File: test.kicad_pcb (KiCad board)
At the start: 4 copper layers, 100 x 50 mm, 110 parts, among them IC1 USBLC6-2SC6, IC2 AD9288BSTZ-40, IC3 MAX17048G+T10, IC4 BQ24074RGTR, IC5 TCA9534APWR, IC6 MCP6S91-E_MS, IC7 MCP6S91-E_MS, IC8 MCP4726A0T-E_CH, J1 PWM, K1 AQY210EHAX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

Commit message: routing
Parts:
- moved SW3 118.0 mm to (114.5, 94.7), turned to 90 degrees
- moved Q1 21.6 mm to (119.0, 85.4)
- moved R15 21.6 mm to (115.5, 86.4)
- moved Q2 21.6 mm to (119.0, 81.8)
- moved R8 21.6 mm to (115.5, 82.8)
- moved R11 20.1 mm to (131.8, 69.6), turned to -90 degrees
- moved IC1 18.4 mm to (113.5, 74.2), turned to 180 degrees
- moved R9 16.5 mm to (134.9, 61.5)
- moved JP1 15.7 mm to (106.9, 66.8), turned to 90 degrees
- moved C15 14.6 mm to (133.2, 61.5)
- moved IC4 12.8 mm to (128.4, 62.6)
- moved C14 12.8 mm to (128.3, 65.6)
- moved C17 12.8 mm to (125.4, 63.1)
- moved R6 11.9 mm to (114.8, 59.3), turned to 90 degrees
- moved R10 11.7 mm to (125.4, 66.5), turned to -90 degrees
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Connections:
- C10 pad 2: GNDA -> GND
- C20 pad 2: GNDA -> GND
- C22 pad 2: GNDA -> GND
- C3 pad 2: GNDA -> GND
- C30 pad 2: GNDA -> GND
- C31 pad 2: GNDA -> GND
- C32 pad 2: GNDA -> GND
- C9 pad 2: GNDA -> GND
- D10 pad 2: GNDA -> GND
- D6 pad 1: GNDA -> GND
- D8 pad 2: GNDA -> GND
- IC2 pad 1: GNDA -> GND
- IC2 pad 10: GNDA -> GNDREF
- IC2 pad 29: GNDA -> GND
- IC2 pad 3: GNDA -> GNDREF
- IC2 pad 32: GNDA -> GND
- IC6 pad 4: GNDA -> GND
- IC7 pad 4: GNDA -> GND
- IC8 pad 2: GNDA -> GND
- R20 pad 1: GNDA -> GND
- R21 pad 1: GNDA -> GND
- U10 pad 4: GNDA -> GND
- U3 pad 13: /CH1_D6 -> /CH2_D6
- U3 pad 14: /CH1_D7 -> /CH2_D7
- U3 pad 24: /CH2_D0 -> /CH1_D7
- U3 pad 26: /CH2_D1 -> /CH1_D6
- U3 pad 27: /CH2_D3 -> /CH1_D5
- U3 pad 28: /CH2_D4 -> /CH1_D4
- U3 pad 29: /CH2_D2 -> /CH1_D3
- U3 pad 30: /CH2_D5 -> /CH1_D2
- U3 pad 31: /CH2_D6 -> /CH1_D1
- U3 pad 37: /CH2_D7 -> /CH1_D0
- U3 pad 4: /CH1_D0 -> /CH2_D0
- U3 pad 5: /CH1_D1 -> /CH2_D1
- U3 pad 6: /CH1_D2 -> /CH2_D2
- U3 pad 7: /CH1_D3 -> /CH2_D3
- U3 pad 8: /CH1_D4 -> /CH2_D4
- U3 pad 9: /CH1_D5 -> /CH2_D5
- U7 pad 1: GNDA -> GND
- U8 pad 4: GNDA -> GND
- U9 pad 4: GNDA -> GND
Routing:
- net GND: track 114.2 -> 320.4 mm, vias 0 -> 28
- net GNDREF: track 69.6 -> 137.4 mm, vias 0 -> 1
- net Net-(C19-Pad1): track 5.91 -> 68.1 mm, vias 0 -> 3
- net Net-(C15-Pad1): track 4.26 -> 64.2 mm, vias 0 -> 1
- net +5V: track 16.2 -> 71.5 mm
- net Offset_CH2: track 3.21 -> 58.3 mm, vias 0 -> 1
- net Offset_CH1: track 3.51 -> 57.5 mm, vias 0 -> 1
- net Trigger_CH1: track 0.00 -> 49.5 mm, vias 0 -> 2
- net Trigger_CH2: track 0.00 -> 48.3 mm, vias 0 -> 2
- net +3V3: track 101.9 -> 148.9 mm, vias 2 -> 9
- net IO0: track 8.03 -> 54.7 mm, vias 0 -> 2
- net Net-(C17-Pad1): track 2.50 -> 48.3 mm, vias 0 -> 3
- net GNDA: track 45.7 -> 0.00 mm, vias 10 -> 0
- net SCL_I2C: track 45.6 -> 89.9 mm, vias 0 -> 4
- net /CH1_D0: track 0.00 -> 40.2 mm, vias 0 -> 2
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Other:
- board text added: "JLCJLCJLC"

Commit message: last changes
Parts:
- removed D10, D9: D_Schottky, Diode_SMD:D_0805_2012Metric_Pad1.15x1.40mm_HandSolder
- added C23: 4.7u, Capacitor_SMD:C_0603_1608Metric_Pad1.08x0.95mm_HandSolder, F.Cu at (123.0, 64.3)
- added G***: LOGO, project_library:test, F.Cu at (111.6, 51.7)
- added TP12: SCLK_I2C, TestPoint:TestPoint_Keystone_5000-5004_Miniature, F.Cu at (158.7, 95.2)
- added TP13: SDA, TestPoint:TestPoint_Keystone_5000-5004_Miniature, F.Cu at (155.2, 95.2)
- added TP14: MOSI, TestPoint:TestPoint_Keystone_5000-5004_Miniature, F.Cu at (169.8, 85.7)
- added TP15: SCLK_SPI, TestPoint:TestPoint_Keystone_5000-5004_Miniature, F.Cu at (162.2, 82.4)
- added TP16: TX, TestPoint:TestPoint_Keystone_5000-5004_Miniature, F.Cu at (118.5, 89.5)
- added TP17: RX, TestPoint:TestPoint_Keystone_5000-5004_Miniature, F.Cu at (122.7, 70.5)
- D7, D8: value D_Schottky -> BAT54S; footprint Diode_SMD:D_0805_2012Metric_Pad1.15x1.40mm_HandSolder -> Package_TO_SOT_SMD:SOT-23
- moved D7 4.88 mm to (190.6, 69.4)
- moved D8 4.09 mm to (190.6, 73.5)
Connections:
- D7 pad 1: +3.3VA -> GND
- D7 pad 2: Net-(C26-Pad1) -> +3.3VA
- D8 pad 1: Net-(C26-Pad1) -> GND
- D8 pad 2: GND -> +3.3VA
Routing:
- net +3V3: track 148.9 -> 107.6 mm
- net SDA: track 84.1 -> 96.1 mm
- net RX: track 26.7 -> 34.3 mm
- net SCL_I2C: track 89.9 -> 97.3 mm
- net MOSI: track 32.7 -> 39.3 mm
- net TX: track 27.4 -> 33.7 mm
- net Net-(IC1-Pad6): track 6.36 -> 12.6 mm, vias 0 -> 2
- net Net-(C17-Pad1): track 48.3 -> 52.7 mm
- net GND: track 320.4 -> 324.5 mm, vias 28 -> 29
- net SCLK_SPI: track 29.3 -> 33.4 mm
- net Net-(C27-Pad1): track 36.7 -> 34.4 mm
- net +5V: track 71.5 -> 70.3 mm
- net +3.3VA: track 68.6 -> 69.4 mm
- net Offset_CH2: track 58.3 -> 59.1 mm
- net Net-(C15-Pad1): track 64.2 -> 64.9 mm
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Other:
- outline, holes or cut-outs redrawn
- board text added: "TH/MO"

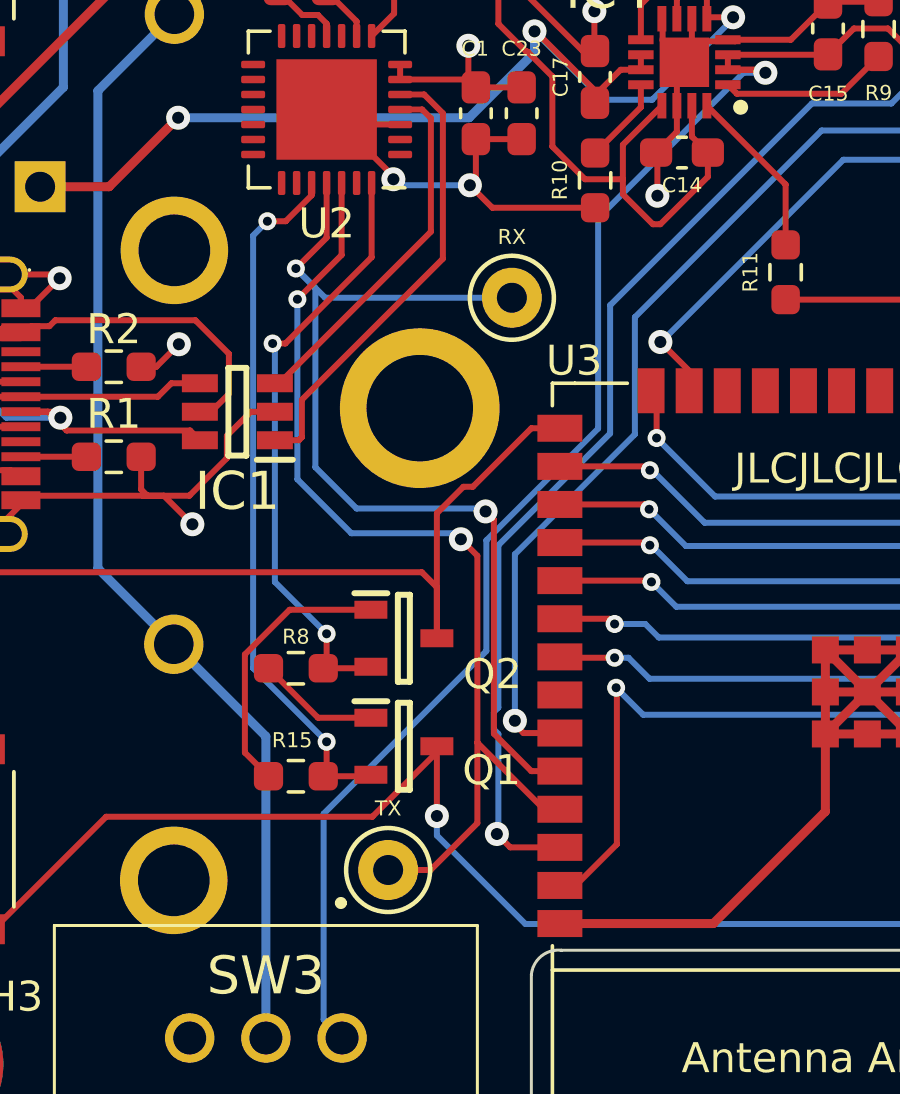
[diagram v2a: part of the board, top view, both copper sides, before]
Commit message: fixed uart connection
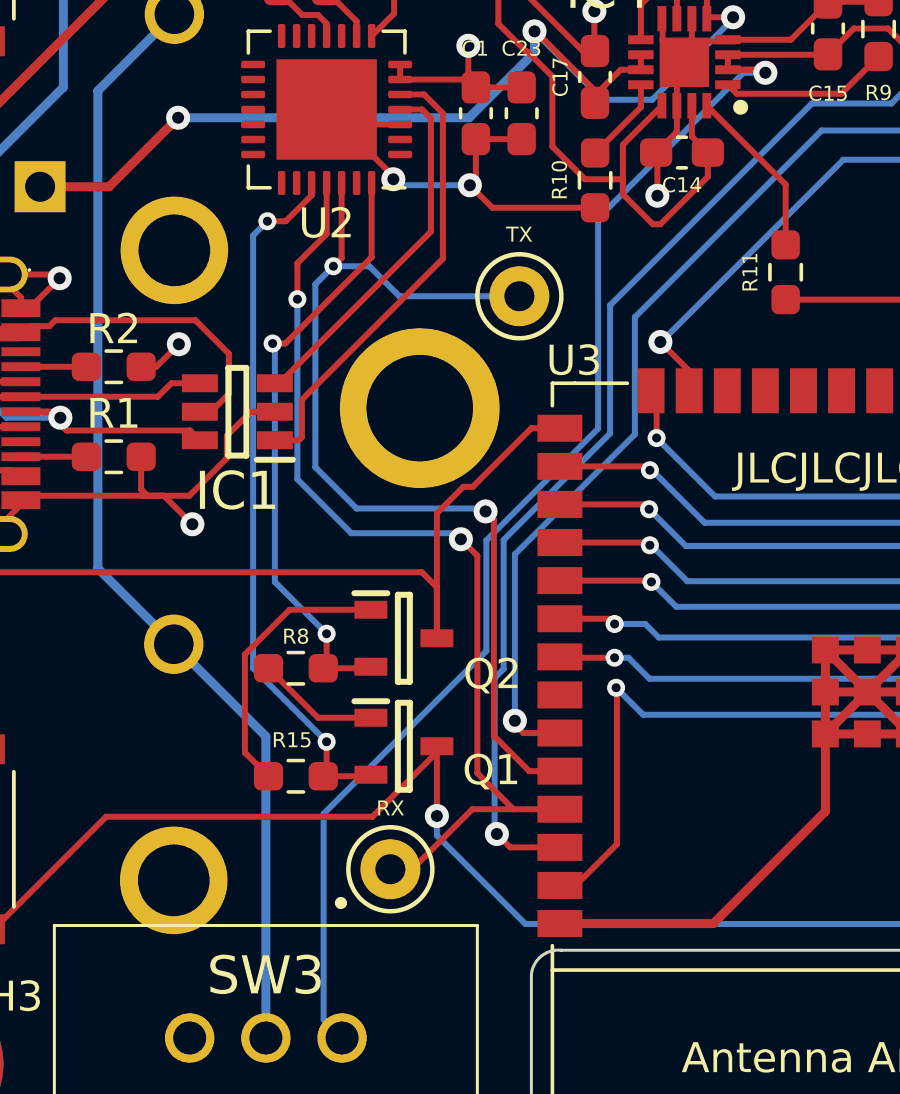
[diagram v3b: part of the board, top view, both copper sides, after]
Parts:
- moved TP16 19.6 mm to (122.9, 70.4)
- moved TP17 19.5 mm to (118.6, 89.5)
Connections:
- U3 pad 34: RX -> TX
- U3 pad 35: TX -> RX
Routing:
- net RX: track 34.3 -> 32.8 mm
- net TX: track 33.7 -> 33.0 mm
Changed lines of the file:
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@@
       (net 46 "SDA") (pinfunction "GPIO21") (pintype "bidirectional"))
     (pad "34" smd rect locked (at 8.75 -1.93) (size 1.5 0.9) (layers "F.Cu" "F.Paste" "F.Mask")
-      (net 5 "RX") (pinfunction "U0RXD/GPIO3") (pintype "bidirectional"))
+      (net 56 "TX") (pinfunction "U0RXD/GPIO3") (pintype "bidirectional"))
     (pad "35" smd rect locked (at 8.75 -3.2) (size 1.5 0.9) (layers "F.Cu" "F.Paste" "F.Mask")
-      (net 56 "TX") (pinfunction "U0TXD/GPIO1") (pintype "bidirectional"))
+      (net 5 "RX") (pinfunction "U0TXD/GPIO1") (pintype "bidirectional"))
     (pad "36" smd rect locked (at 8.75 -4.47) (size 1.5 0.9) (layers "F.Cu" "F.Paste" "F.Mask")
       (net 45 "SCL_I2C") (pinfunction "GPIO22") (pintype "bidirectional"))
@@
   )
   (footprint "TestPoint:TestPoint_Keystone_5000-5004_Miniature" (layer "F.Cu")
-    (at 122.65 70.45)
+    (at 118.6 89.5)
     (descr "Keystone Miniature THM Test Point 5000-5004, http://www.keyelco.com/product-pdf.cfm?p=1309")
     (tags "Through Hole Mount Test Points")
@@
   )
   (footprint "TestPoint:TestPoint_Keystone_5000-5004_Miniature" (layer "F.Cu")
-    (at 118.525 89.525)
+    (at 122.9 70.4)
     (descr "Keystone Miniature THM Test Point 5000-5004, http://www.keyelco.com/product-pdf.cfm?p=1309")
     (tags "Through Hole Mount Test Points")
@@
   (segment (start 150.3 73.1) (end 149.45 72.25) (width 0.2) (layer "In2.Cu") (net 4))
   (segment (start 159.95 73.1) (end 150.3 73.1) (width 0.2) (layer "In2.Cu") (net 4))
-  (segment (start 121.772875 77.572875) (end 122.05 77.85) (width 0.2) (layer "F.Cu") (net 5))
-  (segment (start 122.05 77.85) (end 122.05 84.98) (width 0.2) (layer "F.Cu") (net 5))
-  (segment (start 122.05 84.98) (end 123.3 86.23) (width 0.2) (layer "F.Cu") (net 5))
-  (segment (start 123.3 86.23) (end 124.25 86.23) (width 0.2) (layer "F.Cu") (net 5))
-  (segment (start 115.45 69.475) (end 116.475 68.45) (width 0.2) (layer "F.Cu") (net 5))
-  (segment (start 116.475 68.45) (end 116.475 66.625) (width 0.2) (layer "F.Cu") (net 5))
-  (via (at 115.45 69.475) (size 0.6) (drill 0.3) (layers "F.Cu" "B.Cu") (net 5))
-  (via (at 121.772875 77.572875) (size 0.8) (drill 0.4) (layers "F.Cu" "B.Cu") (net 5))
-  (segment (start 116.099511 70.124511) (end 115.45 69.475) (width 0.2) (layer "B.Cu") (net 5))
-  (segment (start 117.475 77.475) (end 116.099511 76.099511) (width 0.2) (layer "B.Cu") (net 5))
-  (segment (start 116.099511 76.099511) (end 116.099511 70.124511) (width 0.2) (layer "B.Cu") (net 5))
-  (segment (start 121.675 77.475) (end 117.475 77.475) (width 0.2) (layer "B.Cu") (net 5))
-  (segment (start 116.425 70.45) (end 115.45 69.475) (width 0.2) (layer "B.Cu") (net 5))
-  (segment (start 121.772875 77.572875) (end 121.675 77.475) (width 0.2) (layer "B.Cu") (net 5))
-  (segment (start 122.65 70.45) (end 116.425 70.45) (width 0.2) (layer "B.Cu") (net 5))
+  (segment (start 121.5 86.3) (end 121.5 79.05) (width 0.2) (layer "F.Cu") (net 5))
+  (segment (start 122.7 87.5) (end 121.5 86.3) (width 0.2) (layer "F.Cu") (net 5))
+  (segment (start 116.475 68.325) (end 116.475 66.625) (width 0.2) (layer "F.Cu") (net 5))
+  (segment (start 124.25 87.5) (end 122.7 87.5) (width 0.2) (layer "F.Cu") (net 5))
+  (segment (start 115.5 70.5) (end 115.5 69.3) (width 0.2) (layer "F.Cu") (net 5))
+  (segment (start 121.328904 87.5) (end 119.328904 89.5) (width 0.2) (layer "F.Cu") (net 5))
+  (segment (start 115.5 69.3) (end 116.475 68.325) (width 0.2) (layer "F.Cu") (net 5))
+  (segment (start 122.7 87.5) (end 121.328904 87.5) (width 0.2) (layer "F.Cu") (net 5))
+  (segment (start 121.5 79.05) (end 120.95 78.5) (width 0.2) (layer "F.Cu") (net 5))
+  (segment (start 119.328904 89.5) (end 118.6 89.5) (width 0.2) (layer "F.Cu") (net 5))
+  (via (at 115.5 70.5) (size 0.6) (drill 0.3) (layers "F.Cu" "B.Cu") (free) (net 5))
+  (via (at 120.95 78.5) (size 0.8) (drill 0.4) (layers "F.Cu" "B.Cu") (net 5))
+  (segment (start 115.5 76.5) (end 115.5 70.5) (width 0.2) (layer "B.Cu") (net 5))
+  (segment (start 120.95 78.5) (end 120.75 78.3) (width 0.2) (layer "B.Cu") (net 5))
+  (segment (start 120.75 78.3) (end 117.3 78.3) (width 0.2) (layer "B.Cu") (net 5))
+  (segment (start 117.3 78.3) (end 115.5 76.5) (width 0.2) (layer "B.Cu") (net 5))
   (segment (start 156.53 74.742) (end 156.53 73.0375) (width 0.2) (layer "F.Cu") (net 6))
   (segment (start 165.5 62.2) (end 165.5 61.803) (width 0.2) (layer "F.Cu") (net 6))
@@
   (via (at 146.612511 59) (size 0.6) (drill 0.3) (layers "F.Cu" "B.Cu") (net 45))
   (segment (start 138.575 60.7) (end 138.575 60.525) (width 0.2) (layer "B.Cu") (net 45))
-  (segment (start 122.2 84.110241) (end 122.2 78.7) (width 0.2) (layer "B.Cu") (net 45))
-  (segment (start 122.2 78.7) (end 125.925 74.975) (width 0.2) (layer "B.Cu") (net 45))
   (segment (start 125.925 70.7) (end 132.65 63.975) (width 0.2) (layer "B.Cu") (net 45))
-  (segment (start 122.049989 84.839748) (end 122.049989 84.260252) (width 0.2) (layer "B.Cu") (net 45))
-  (segment (start 125.925 74.975) (end 125.925 70.7) (width 0.2) (layer "B.Cu") (net 45))
-  (segment (start 122.2 84.989759) (end 122.049989 84.839748) (width 0.2) (layer "B.Cu") (net 45))
-  (segment (start 122.049989 84.260252) (end 122.2 84.110241) (width 0.2) (layer "B.Cu") (net 45))
-  (segment (start 135.3 63.975) (end 138.575 60.7) (width 0.2) (layer "B.Cu") (net 45))
-  (segment (start 122.15 88.325) (end 122.2 88.275) (width 0.2) (layer "B.Cu") (net 45))
-  (segment (start 122.2 88.275) (end 122.2 84.989759) (width 0.2) (layer "B.Cu") (net 45))
+  (segment (start 122.15 88.325) (end 122.074989 88.249989) (width 0.2) (layer "B.Cu") (net 45))
   (segment (start 132.65 63.975) (end 135.3 63.975) (width 0.2) (layer "B.Cu") (net 45))
+  (segment (start 122.37498 78.52502) (end 125.925 74.975) (width 0.2) (layer "B.Cu") (net 45))
+  (segment (start 135.3 63.975) (end 138.575 60.7) (width 0.2) (layer "B.Cu") (net 45))
+  (segment (start 125.925 74.975) (end 125.925 70.7) (width 0.2) (layer "B.Cu") (net 45))
+  (segment (start 122.074989 83.125011) (end 122.37498 82.82502) (width 0.2) (layer "B.Cu") (net 45))
   (segment (start 146.612511 59) (end 148.45 59) (width 0.2) (layer "B.Cu") (net 45))
+  (segment (start 122.37498 82.82502) (end 122.37498 78.52502) (width 0.2) (layer "B.Cu") (net 45))
+  (segment (start 122.074989 88.249989) (end 122.074989 83.125011) (width 0.2) (layer "B.Cu") (net 45))
   (segment (start 144.886411 59.861411) (end 145.423911 59.861411) (width 0.2) (layer "F.Cu") (net 46))
   (segment (start 160.624511 73.379393) (end 160.624511 69.805989) (width 0.2) (layer "F.Cu") (net 46))
@@
   (segment (start 164.774511 67.539748) (end 164.164259 68.15) (width 0.2) (layer "B.Cu") (net 55))
   (segment (start 164.164259 68.15) (end 155.25 68.15) (width 0.2) (layer "B.Cu") (net 55))
-  (segment (start 118.525 89.525) (end 119.939213 89.525) (width 0.2) (layer "F.Cu") (net 56))
-  (segment (start 121.5 85.279022) (end 123.720978 87.5) (width 0.2) (layer "F.Cu") (net 56))
-  (segment (start 123.720978 87.5) (end 124.25 87.5) (width 0.2) (layer "F.Cu") (net 56))
-  (segment (start 120.95 78.5) (end 121.5 79.05) (width 0.2) (layer "F.Cu") (net 56))
-  (segment (start 115.5 70.5) (end 116.975 69.025) (width 0.2) (layer "F.Cu") (net 56))
-  (segment (start 121.5 87.964213) (end 121.5 85.279022) (width 0.2) (layer "F.Cu") (net 56))
-  (segment (start 119.939213 89.525) (end 121.5 87.964213) (width 0.2) (layer "F.Cu") (net 56))
-  (segment (start 116.975 69.025) (end 116.975 66.625) (width 0.2) (layer "F.Cu") (net 56))
-  (segment (start 121.5 79.05) (end 121.5 85.279022) (width 0.2) (layer "F.Cu") (net 56))
-  (via (at 115.5 70.5) (size 0.6) (drill 0.3) (layers "F.Cu" "B.Cu") (net 56))
-  (via (at 120.95 78.5) (size 0.8) (drill 0.4) (layers "F.Cu" "B.Cu") (net 56))
-  (segment (start 115.5 76.5) (end 115.5 70.5) (width 0.2) (layer "B.Cu") (net 56))
-  (segment (start 120.95 78.5) (end 120.75 78.3) (width 0.2) (layer "B.Cu") (net 56))
-  (segment (start 120.75 78.3) (end 117.3 78.3) (width 0.2) (layer "B.Cu") (net 56))
-  (segment (start 117.3 78.3) (end 115.5 76.5) (width 0.2) (layer "B.Cu") (net 56))
+  (segment (start 116.7 69.4) (end 116.975 69.125) (width 0.2) (layer "F.Cu") (net 56))
+  (segment (start 122.05 77.85) (end 121.772875 77.572875) (width 0.2) (layer "F.Cu") (net 56))
+  (segment (start 123.23 86.23) (end 122.05 85.05) (width 0.2) (layer "F.Cu") (net 56))
+  (segment (start 124.25 86.23) (end 123.23 86.23) (width 0.2) (layer "F.Cu") (net 56))
+  (segment (start 116.975 69.125) (end 116.975 66.625) (width 0.2) (layer "F.Cu") (net 56))
+  (segment (start 122.05 85.05) (end 122.05 77.85) (width 0.2) (layer "F.Cu") (net 56))
+  (via (at 116.7 69.4) (size 0.6) (drill 0.3) (layers "F.Cu" "B.Cu") (free) (net 56))
+  (via (at 121.772875 77.572875) (size 0.8) (drill 0.4) (layers "F.Cu" "B.Cu") (net 56))
+  (segment (start 118.9 70.4) (end 122.9 70.4) (width 0.2) (layer "B.Cu") (net 56))
+  (segment (start 116.7 69.4) (end 116.099511 70.000489) (width 0.2) (layer "B.Cu") (net 56))
+  (segment (start 121.675 77.475) (end 121.772875 77.572875) (width 0.2) (layer "B.Cu") (net 56))
+  (segment (start 116.099511 70.000489) (end 116.099511 76.099511) (width 0.2) (layer "B.Cu") (net 56))
+  (segment (start 117.475 77.475) (end 121.675 77.475) (width 0.2) (layer "B.Cu") (net 56))
+  (segment (start 117.9 69.4) (end 118.9 70.4) (width 0.2) (layer "B.Cu") (net 56))
+  (segment (start 116.7 69.4) (end 117.9 69.4) (width 0.2) (layer "B.Cu") (net 56))
+  (segment (start 116.099511 76.099511) (end 117.475 77.475) (width 0.2) (layer "B.Cu") (net 56))
   (segment (start 180.975 59.93) (end 181.1 59.805) (width 0.3) (layer "F.Cu") (net 57))
   (segment (start 180.975 62.4) (end 180.975 59.93) (width 0.3) (layer "F.Cu") (net 57))
